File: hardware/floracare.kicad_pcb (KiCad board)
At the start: 2 copper layers, 100 x 100 mm, 25 parts, among them J2 Conn_01x04_Socket, J4 Conn_01x04_Socket, J5 Conn_01x14_Socket, J6 Conn_01x05_Socket, SW1 SW_Push, SW2 SW_Push, U1 AMS1117-3.3, U2 ESP32-S3-WROOM-1

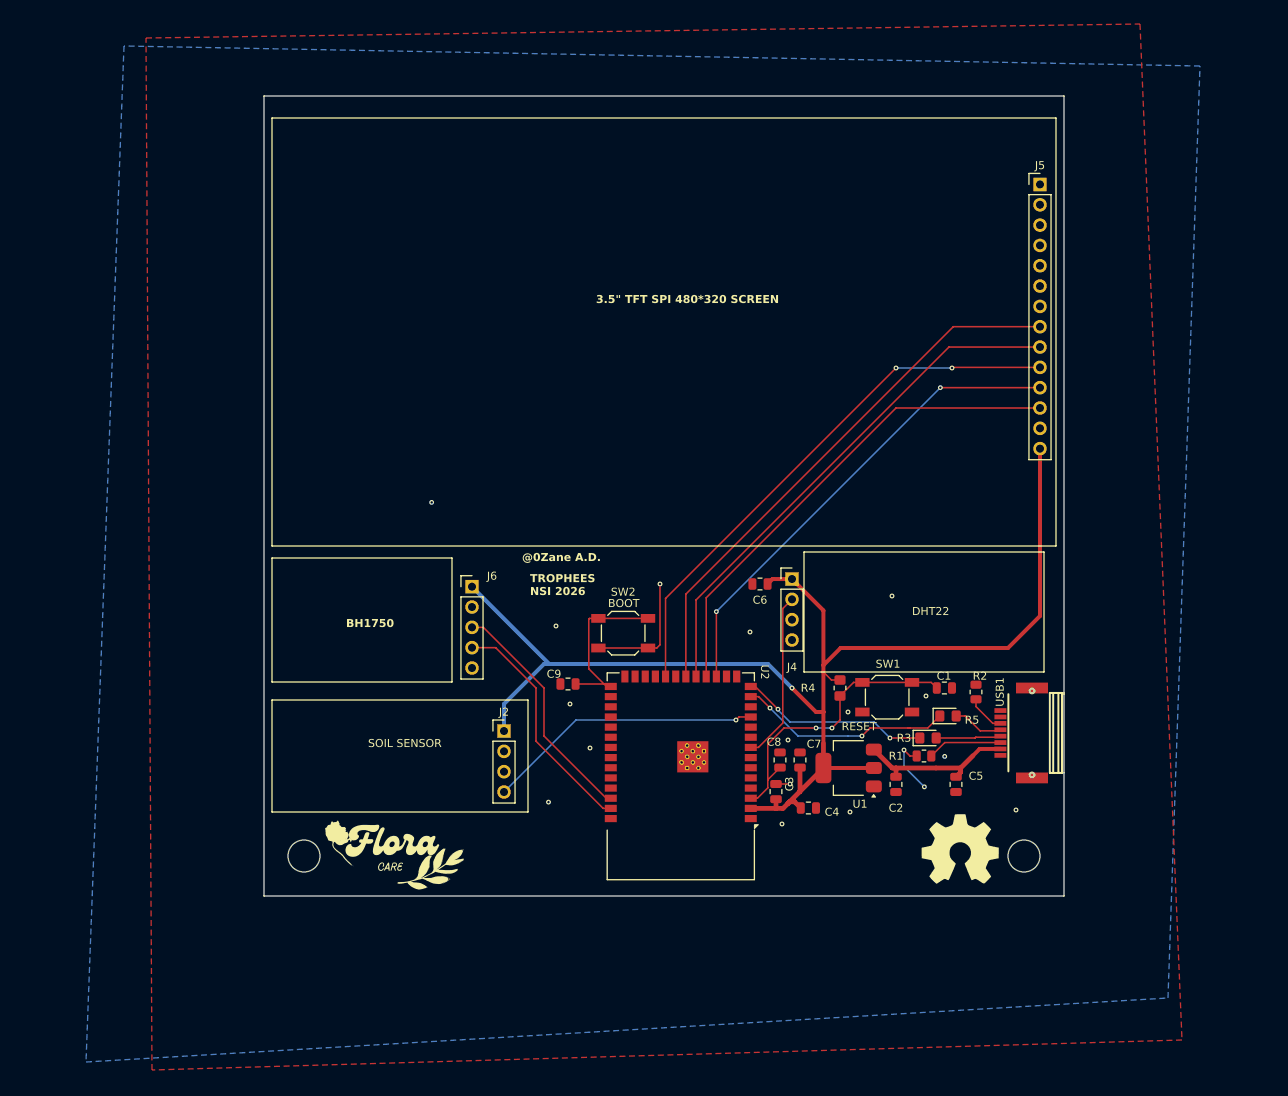
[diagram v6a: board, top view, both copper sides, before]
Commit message: Finishing USB-C Routing & PCB [DRC STABLE]
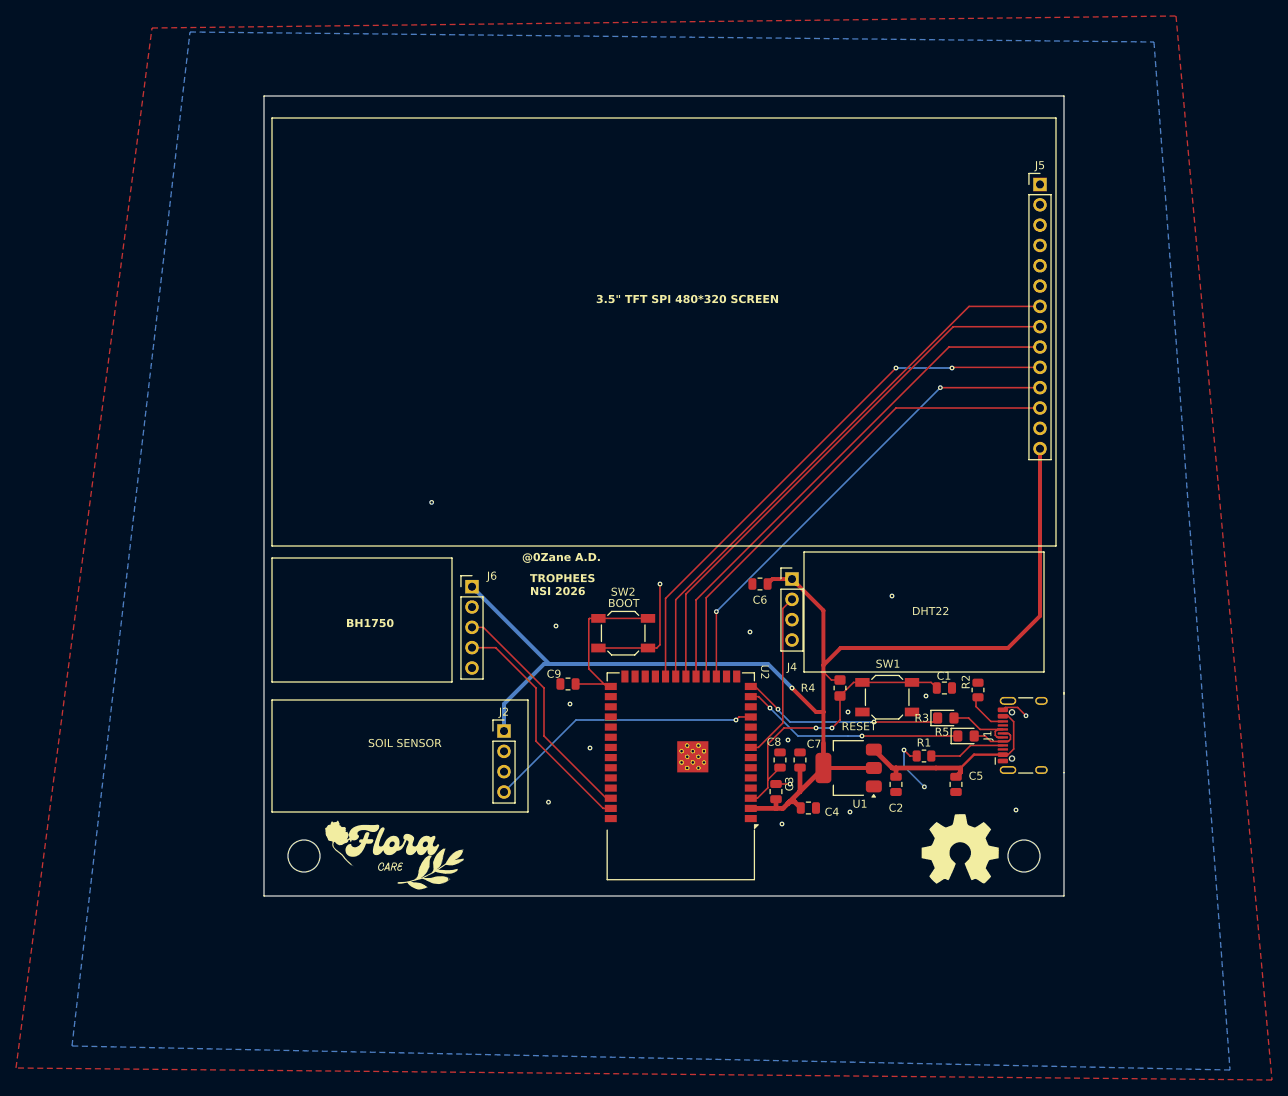
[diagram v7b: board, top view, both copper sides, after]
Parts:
- removed USB1: GT-USB-7100A, easyeda2kicad:USB-C-SMD_GT-USB-7100A
- added J1: USB_C_Receptacle_USB2.0_16P, Connector_USB:USB_C_Receptacle_HCTL_HC-TYPE-C-16P-01A, F.Cu at (236.5, 105.8)
- moved R5 3.36 mm to (228.2, 105.8)
- moved R3 3.35 mm to (225.6, 103.6)
- moved R2 0.35 mm to (229.7, 100.1)
- turned R1 to 0 degrees
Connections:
- R1 pad 1: Net-(USB1-CC1) -> GND
- R1 pad 2: GND -> Net-(J1-CC1)
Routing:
- net LED: track 0.00 -> 70.3 mm
- net Net-(J1-CC1): track 0.00 -> 9.49 mm
- net Net-(USB1-CC1): track 9.33 -> 0.00 mm
- net +5V: track 20.3 -> 26.9 mm
- net GND: track 24.8 -> 28.2 mm
- net Net-(U2-USB_D+): track 23.9 -> 25.5 mm
- net Net-(U2-USB_D-): track 26.9 -> 27.9 mm
- net DATA+: track 8.49 -> 9.29 mm
